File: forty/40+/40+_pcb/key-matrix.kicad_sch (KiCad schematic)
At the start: 48 parts

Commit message: macro w/ pcb start
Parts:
- added D26, D27, D28, D29, D30, D31, D32, D33, D34, D35, D36, D37, D38, D39, D40, D41, D42, D43, D44, D45, D46, D47, D48, D49, D50, D51, D52, D56, D60, D61, D62: Diode, symbol ScottoKeebs:Placeholder_Diode
- added S25, S26, S27, S28, S29, S30, S31, S32, S33, S34, S35, S36, S37, S38, S39, S40, S41, S42, S43, S44, S45, S46, S47, S48, S49, S50, S51, S55, S59, S60, S61: Keyswitch, MX_Alps_Hybrid:MX-Alps-Hybrid-1U, symbol ScottoKeebs:Placeholder_Keyswitch
- S1, S10, S11, S12, S13, S14, S15, S16, S17, S18, S19, S2, S20, S21, S22, S23, S24, S3, S4, S5, S6, S7, S8, S9: footprint (none) -> MX_Alps_Hybrid:MX-Alps-Hybrid-1U
- renumbered D9 to D10, D10 to D11, D11 to D12, D12 to D13, D13 to D14, D14 to D15, D15 to D16, D16 to D17, D17 to D18, D18 to D19, D1 to D2, D19 to D20, D20 to D21, D21 to D22, D22 to D23, D23 to D24, D24 to D25, D2 to D3, D3 to D4, D4 to D5, D5 to D6, D6 to D7, D7 to D8, D8 to D9
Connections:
- net at S18.1: now also S2.1, S33.1, S48.1
- net at D5.1 (K): now also D10.1 (K), D11.1 (K), D12.1 (K), D13.1 (K), D14.1 (K), D15.1 (K), D16.1 (K), D17.1 (K), D2.1 (K), D3.1 (K), D4.1 (K), D6.1 (K), D7.1 (K), D8.1 (K), D9.1 (K)
- net at S8.1: now also S24.1, S39.1
- net at S23.1: now also S7.1, S38.1
- net at D18.1 (K): now also D19.1 (K), D20.1 (K), D21.1 (K), D22.1 (K), D23.1 (K), D24.1 (K), D25.1 (K), D26.1 (K), D27.1 (K), D28.1 (K), D29.1 (K), D30.1 (K), D31.1 (K), D32.1 (K)
- net at S15.1: now also S31.1, S47.1, S61.1
- net at S22.1: now also S6.1, S37.1
- net at S14.1: now also S30.1, S45.1, S60.1
- net at S11.1: now also S27.1, S42.1
- net at S10.1: now also S26.1, S41.1
- net at S13.1: now also S29.1, S44.1, S59.1
- net at S1.1: now also S17.1, S32.1, S46.1
- net at S19.1: now also S3.1, S34.1, S49.1
- net at S5.1: now also S21.1, S36.1, S51.1
- net at S9.1: now also S25.1, S40.1, S55.1
- net at S12.1: now also S28.1, S43.1
- net at S20.1: now also S4.1, S35.1, S50.1
- new net: D29.2 (A), S28.2
- new net: D62.2 (A), S61.2
- new net: D45.2 (A), S44.2
- new net: D34.2 (A), S33.2
- new net: D28.2 (A), S27.2
- new net: D33.1 (K), D34.1 (K), D35.1 (K), D36.1 (K), D37.1 (K), D38.1 (K), D39.1 (K), D40.1 (K), D41.1 (K), D42.1 (K), D43.1 (K), D44.1 (K), D45.1 (K), D46.1 (K), D48.1 (K)
- new net: D41.2 (A), S40.2
- new net: D46.2 (A), S45.2
- new net: D30.2 (A), S29.2
- new net: D44.2 (A), S43.2
- new net: D56.2 (A), S55.2
- new net: D43.2 (A), S42.2
- new net: D47.1 (K), D49.1 (K), D50.1 (K), D51.1 (K), D52.1 (K), D56.1 (K), D60.1 (K), D61.1 (K), D62.1 (K)
- new net: D47.2 (A), S46.2
- new net: D37.2 (A), S36.2
- new net: D60.2 (A), S59.2
- new net: D32.2 (A), S31.2
- new net: D35.2 (A), S34.2
- new net: D49.2 (A), S48.2
- new net: D52.2 (A), S51.2
- new net: D31.2 (A), S30.2
- new net: D50.2 (A), S49.2
- new net: D61.2 (A), S60.2
- new net: D36.2 (A), S35.2
- new net: D27.2 (A), S26.2
- new net: D26.2 (A), S25.2
- new net: D33.2 (A), S32.2
- new net: D42.2 (A), S41.2
- new net: D48.2 (A), S47.2
- new net: D38.2 (A), S37.2
- new net: D40.2 (A), S39.2
- new net: D39.2 (A), S38.2
- new net: D51.2 (A), S50.2
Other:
- moved on the sheet: D10, D11, D12, D13, D14, D15, D16, D17, D18, D19, D2, D20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

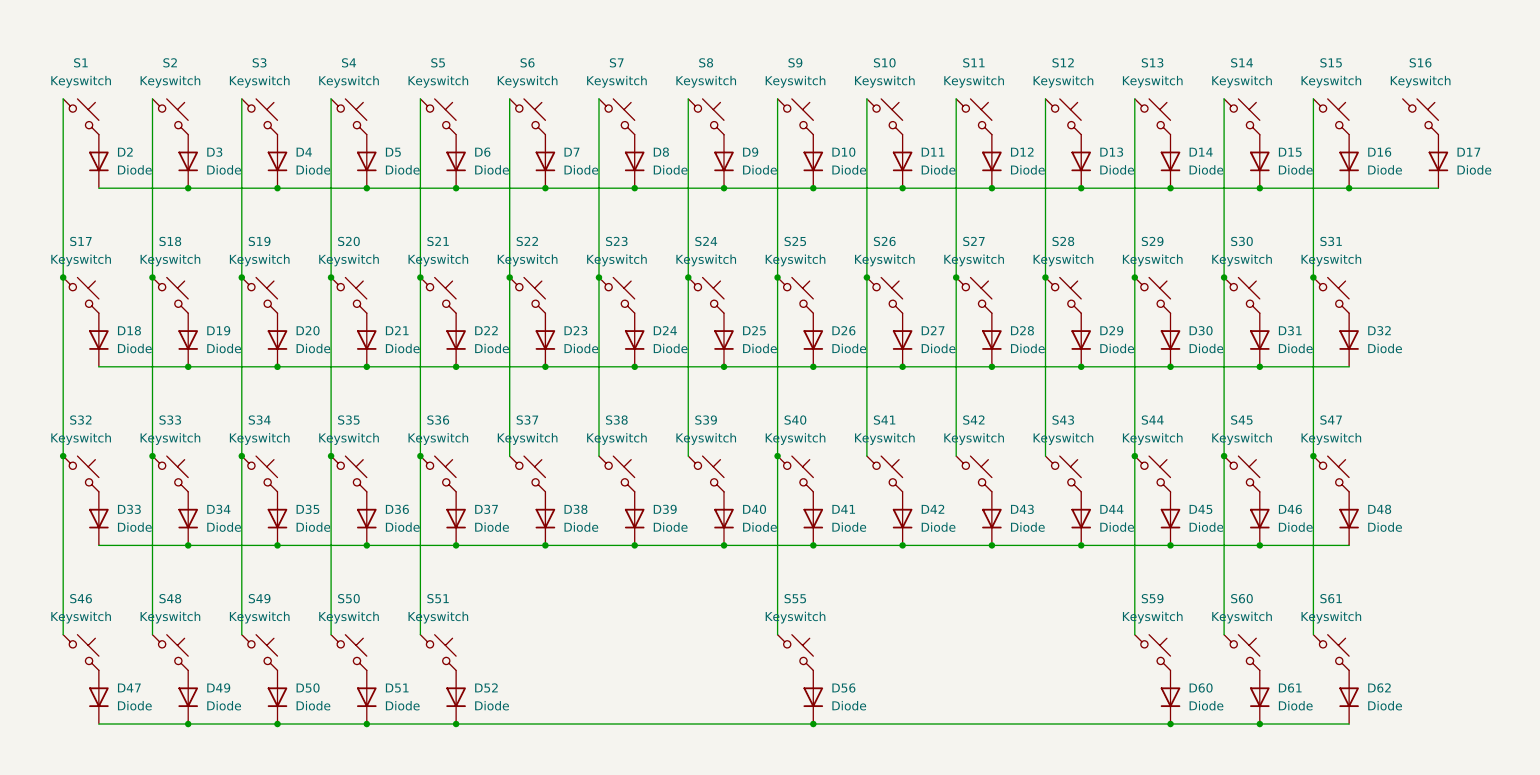
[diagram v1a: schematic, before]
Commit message: Add 40%+ keyboard layout and update PCB files
Added a new 40%+ keyboard layout JSON with function keys, updated and added KiCad PCB, schematic, and project files for the 40+ PCB, and included new backup and log files. Also added the nRF52840 spec sheet and made changes to the macropad PCB project file.
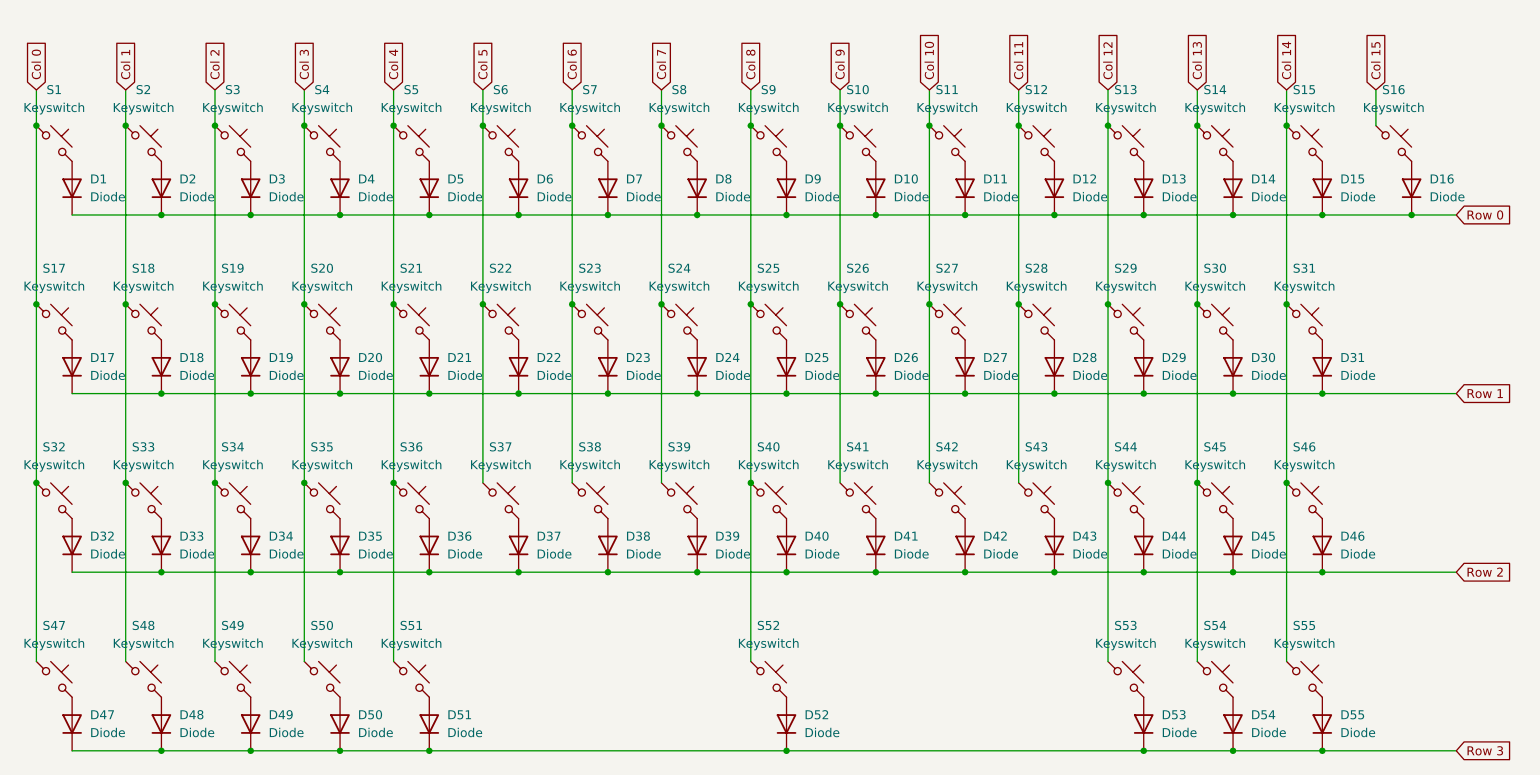
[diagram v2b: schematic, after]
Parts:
- D1: renamed from D2; footprint (none) -> Diode_SMD:D_SOD-123
- D10: renamed from D11; footprint (none) -> Diode_SMD:D_SOD-123
- D11: renamed from D12; footprint (none) -> Diode_SMD:D_SOD-123
- D12: renamed from D13; footprint (none) -> Diode_SMD:D_SOD-123
- D13: renamed from D14; footprint (none) -> Diode_SMD:D_SOD-123
- D14: renamed from D15; footprint (none) -> Diode_SMD:D_SOD-123
- D15: renamed from D16; footprint (none) -> Diode_SMD:D_SOD-123
- D16: renamed from D17; footprint (none) -> Diode_SMD:D_SOD-123
- D17: renamed from D18; footprint (none) -> Diode_SMD:D_SOD-123
- D18: renamed from D19; footprint (none) -> Diode_SMD:D_SOD-123
- D19: renamed from D20; footprint (none) -> Diode_SMD:D_SOD-123
- D2: renamed from D3; footprint (none) -> Diode_SMD:D_SOD-123
- D20: renamed from D21; footprint (none) -> Diode_SMD:D_SOD-123
- D21: renamed from D22; footprint (none) -> Diode_SMD:D_SOD-123
- D22: renamed from D23; footprint (none) -> Diode_SMD:D_SOD-123
- D23: renamed from D24; footprint (none) -> Diode_SMD:D_SOD-123
- D24: renamed from D25; footprint (none) -> Diode_SMD:D_SOD-123
- D25: renamed from D26; footprint (none) -> Diode_SMD:D_SOD-123
- D26: renamed from D27; footprint (none) -> Diode_SMD:D_SOD-123
- D27: renamed from D28; footprint (none) -> Diode_SMD:D_SOD-123
- D28: renamed from D29; footprint (none) -> Diode_SMD:D_SOD-123
- D29: renamed from D30; footprint (none) -> Diode_SMD:D_SOD-123
- D3: renamed from D4; footprint (none) -> Diode_SMD:D_SOD-123
- D30: renamed from D31; footprint (none) -> Diode_SMD:D_SOD-123
- D31: renamed from D32; footprint (none) -> Diode_SMD:D_SOD-123
- D32: renamed from D33; footprint (none) -> Diode_SMD:D_SOD-123
- D33: renamed from D34; footprint (none) -> Diode_SMD:D_SOD-123
- D34: renamed from D35; footprint (none) -> Diode_SMD:D_SOD-123
- D35: renamed from D36; footprint (none) -> Diode_SMD:D_SOD-123
- D36: renamed from D37; footprint (none) -> Diode_SMD:D_SOD-123
- D37: renamed from D38; footprint (none) -> Diode_SMD:D_SOD-123
- D38: renamed from D39; footprint (none) -> Diode_SMD:D_SOD-123
- D39: renamed from D40; footprint (none) -> Diode_SMD:D_SOD-123
- D4: renamed from D5; footprint (none) -> Diode_SMD:D_SOD-123
- D40: renamed from D41; footprint (none) -> Diode_SMD:D_SOD-123
- D41: renamed from D42; footprint (none) -> Diode_SMD:D_SOD-123
- D42: renamed from D43; footprint (none) -> Diode_SMD:D_SOD-123
- D43: renamed from D44; footprint (none) -> Diode_SMD:D_SOD-123
- D44: renamed from D45; footprint (none) -> Diode_SMD:D_SOD-123
- D45: renamed from D46; footprint (none) -> Diode_SMD:D_SOD-123
- D46: renamed from D48; footprint (none) -> Diode_SMD:D_SOD-123
- D47: footprint (none) -> Diode_SMD:D_SOD-123
- D48: renamed from D49; footprint (none) -> Diode_SMD:D_SOD-123
- D49: renamed from D50; footprint (none) -> Diode_SMD:D_SOD-123
- D5: renamed from D6; footprint (none) -> Diode_SMD:D_SOD-123
- D50: renamed from D51; footprint (none) -> Diode_SMD:D_SOD-123
- D51: renamed from D52; footprint (none) -> Diode_SMD:D_SOD-123
- D52: renamed from D56; footprint (none) -> Diode_SMD:D_SOD-123
- D53: renamed from D60; footprint (none) -> Diode_SMD:D_SOD-123
- D54: renamed from D61; footprint (none) -> Diode_SMD:D_SOD-123
- D55: renamed from D62; footprint (none) -> Diode_SMD:D_SOD-123
- D6: renamed from D7; footprint (none) -> Diode_SMD:D_SOD-123
- D7: renamed from D8; footprint (none) -> Diode_SMD:D_SOD-123
- D8: renamed from D9; footprint (none) -> Diode_SMD:D_SOD-123
- D9: renamed from D10; footprint (none) -> Diode_SMD:D_SOD-123
- renumbered S47 to S46, S46 to S47, S55 to S52, S59 to S53, S60 to S54, S61 to S55
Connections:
- net Col 1: now reaches S18.1, S2.1, S33.1, S48.1
- net Col 11: now reaches S12.1, S28.1, S43.1
- net Row 0: now reaches D1.1 (K), D10.1 (K), D11.1 (K), D12.1 (K), D13.1 (K), D14.1 (K), D15.1 (K), D16.1 (K), D2.1 (K), D3.1 (K), D4.1 (K), D5.1 (K), D6.1 (K), D7.1 (K), D8.1 (K), D9.1 (K)
- net Col 14: now reaches S15.1, S31.1, S46.1, S55.1
- net Col 12: now reaches S13.1, S29.1, S44.1, S53.1
- net Col 10: now reaches S11.1, S27.1, S42.1
- net Row 2: now reaches D32.1 (K), D33.1 (K), D34.1 (K), D35.1 (K), D36.1 (K), D37.1 (K), D38.1 (K), D39.1 (K), D40.1 (K), D41.1 (K), D42.1 (K), D43.1 (K), D44.1 (K), D45.1 (K), D46.1 (K)
- net Col 8: now reaches S25.1, S40.1, S52.1, S9.1
- net Col 7: now reaches S24.1, S39.1, S8.1
- net Row 3: now reaches D47.1 (K), D48.1 (K), D49.1 (K), D50.1 (K), D51.1 (K), D52.1 (K), D53.1 (K), D54.1 (K), D55.1 (K)
- net Col 6: now reaches S23.1, S38.1, S7.1
- net Row 1: now reaches D17.1 (K), D18.1 (K), D19.1 (K), D20.1 (K), D21.1 (K), D22.1 (K), D23.1 (K), D24.1 (K), D25.1 (K), D26.1 (K), D27.1 (K), D28.1 (K), D29.1 (K), D30.1 (K), D31.1 (K)
- net Col 0: now reaches S1.1, S17.1, S32.1, S47.1
- net Col 4: now reaches S21.1, S36.1, S5.1, S51.1
- net Col 5: now reaches S22.1, S37.1, S6.1
- net Col 13: now reaches S14.1, S30.1, S45.1, S54.1
- net Col 2: now reaches S19.1, S3.1, S34.1, S49.1
- net Col 9: now reaches S10.1, S26.1, S41.1
- net Col 15: now reaches S16.1
- net Col 3: now reaches S20.1, S35.1, S4.1, S50.1
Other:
- moved on the sheet: D1, D10, D11, D12, D13, D14, D15, D16, D17, D18, D19, D2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
